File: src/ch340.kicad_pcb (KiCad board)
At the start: 2 copper layers, 43.2 x 19.2 mm, 17 parts, among them J1 USB_A, J2 Conn_01x04_Male, U1 CH340C, U2 662K

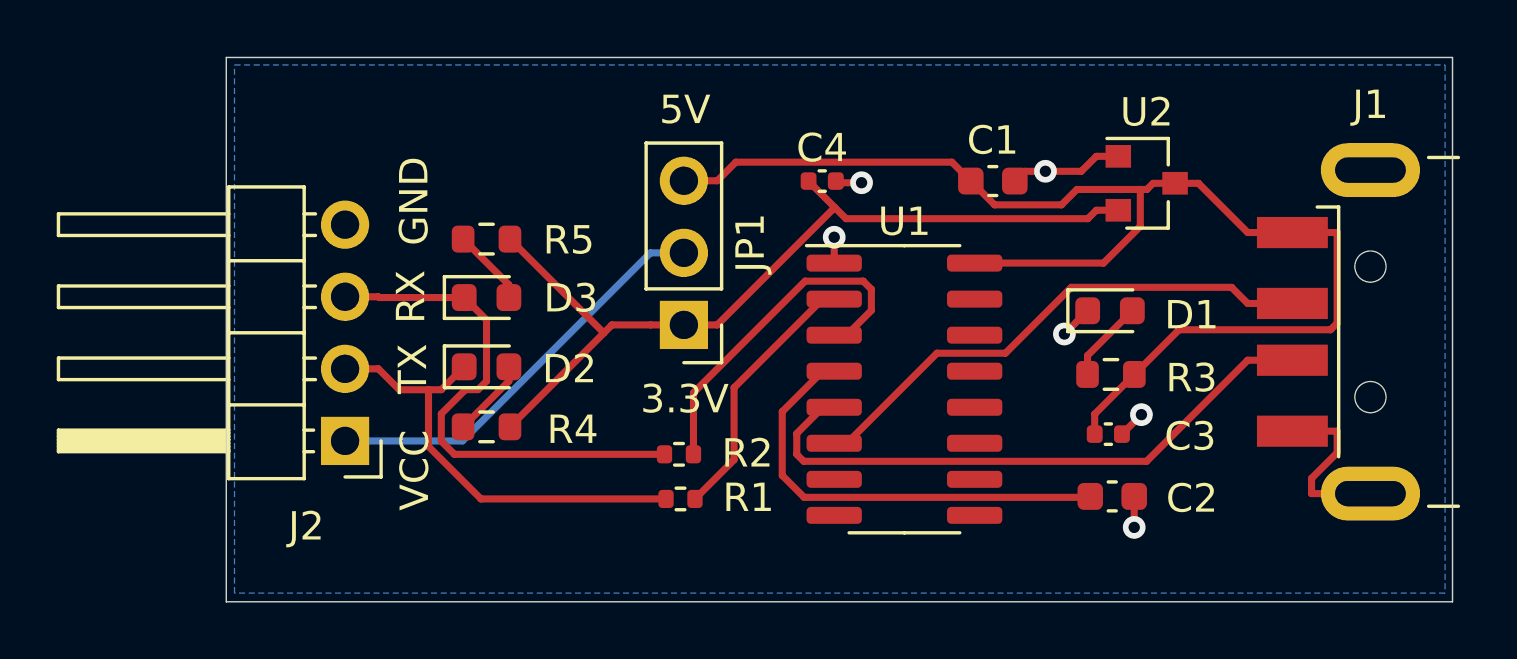
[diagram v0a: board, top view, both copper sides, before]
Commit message: 1. set track width of GND, VCC 0.5mm 2. add vias to GND 3. change footprint, 0403 to 0603 handsoldering
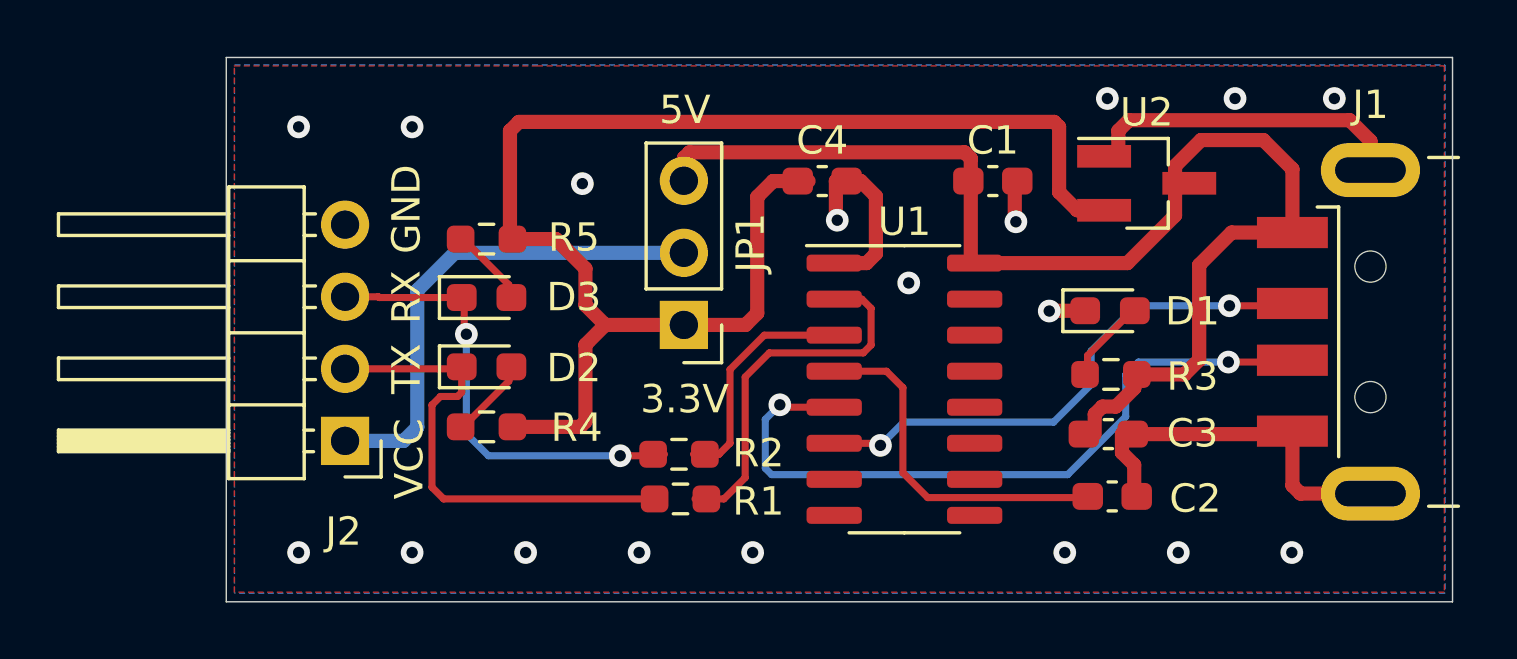
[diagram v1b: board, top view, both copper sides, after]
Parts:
- C1, C2: footprint Capacitor_SMD:C_0603_1608Metric -> Capacitor_SMD:C_0603_1608Metric_Pad1.08x0.95mm_HandSolder
- C3, C4: footprint Capacitor_SMD:C_0402_1005Metric -> Capacitor_SMD:C_0603_1608Metric_Pad1.08x0.95mm_HandSolder
- D1, D2, D3: footprint LED_SMD:LED_0603_1608Metric -> LED_SMD:LED_0603_1608Metric_Pad1.05x0.95mm_HandSolder
- R1, R2: footprint Resistor_SMD:R_0402_1005Metric -> Resistor_SMD:R_0603_1608Metric_Pad0.98x0.95mm_HandSolder
- R3, R4, R5: footprint Resistor_SMD:R_0603_1608Metric -> Resistor_SMD:R_0603_1608Metric_Pad0.98x0.95mm_HandSolder
- U2: footprint Package_TO_SOT_SMD:SOT-23 -> Package_TO_SOT_SMD:SOT-23_Handsoldering
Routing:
- net /3.3V: track 30.9 -> 51.0 mm
- net GND: track 15.3 -> 34.0 mm, vias 6 -> 18
- net Net-(R2-Pad2): track 12.6 -> 8.22 mm
- net Net-(J1-Pad3): track 21.5 -> 25.6 mm, vias 0 -> 2
- net Net-(R1-Pad2): track 9.31 -> 13.3 mm
- net Net-(C2-Pad1): track 15.9 -> 12.6 mm
- net Net-(J2-Pad1): track 14.7 -> 17.5 mm
- net VBUS: track 46.4 -> 44.2 mm
- net /RX: track 18.6 -> 16.4 mm, vias 0 -> 2
- net /TX: track 16.0 -> 17.2 mm
- net Net-(J1-Pad2): track 18.7 -> 18.9 mm, vias 0 -> 2
- added copper zone on F.Cu, net GND

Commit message: 更新布线
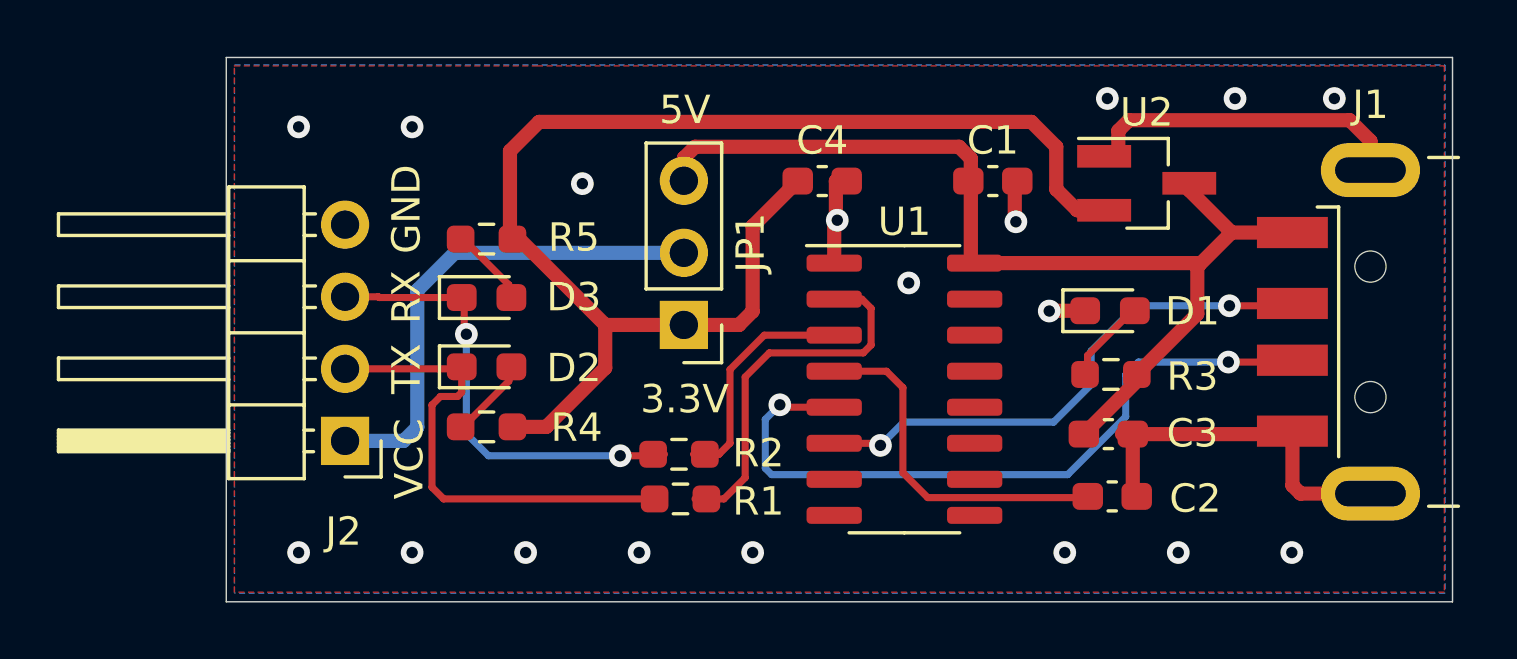
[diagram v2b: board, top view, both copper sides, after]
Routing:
- net VBUS: track 44.2 -> 37.2 mm
- net GND: track 34.0 -> 30.2 mm
- net /3.3V: track 51.0 -> 47.4 mm
